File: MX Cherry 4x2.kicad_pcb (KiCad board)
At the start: 2 copper layers, 78.7 x 38.1 mm, 18 parts, among them J1 Conn_01x10_Pin, J2 Conn_01x10_Pin, SW1 SW_Push, SW2 SW_Push, SW3 SW_Push, SW4 SW_Push, SW5 SW_Push, SW6 SW_Push, SW7 SW_Push, SW8 SW_Push

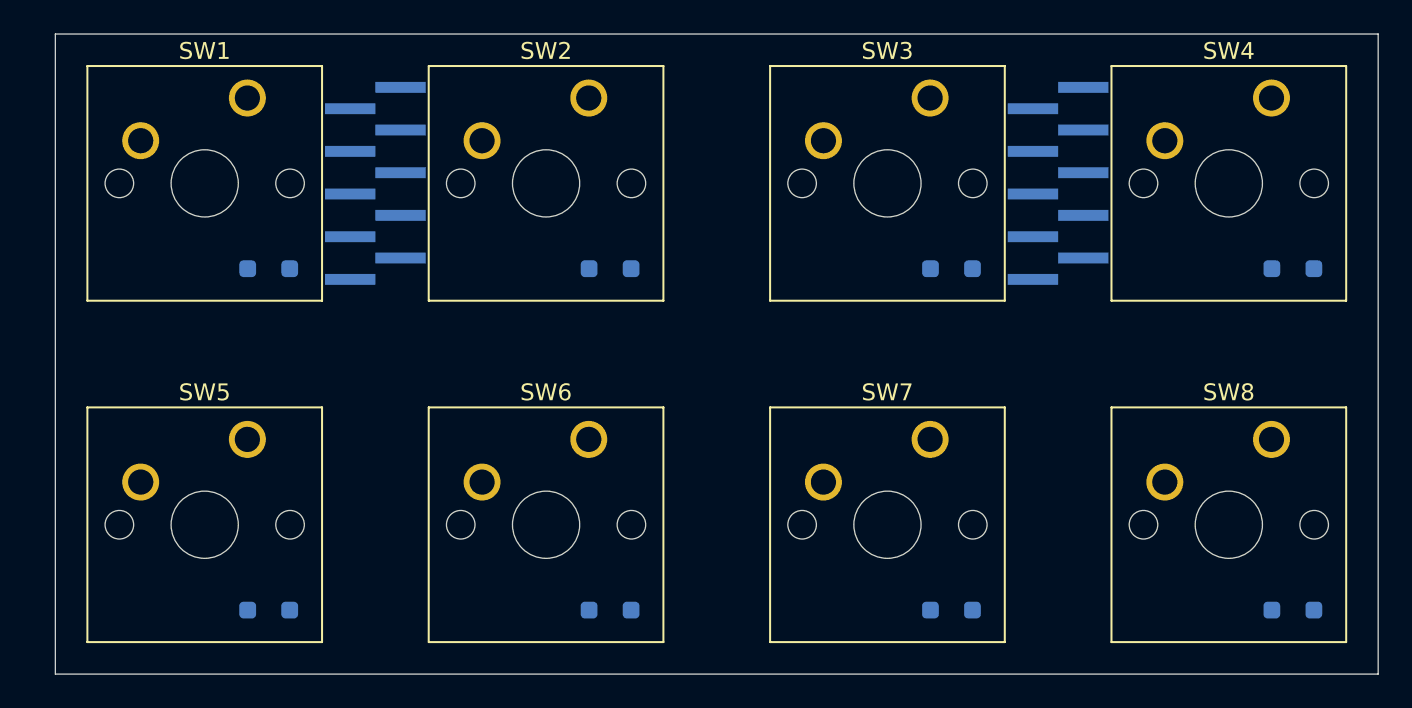
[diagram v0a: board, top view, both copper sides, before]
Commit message: Add LEDs
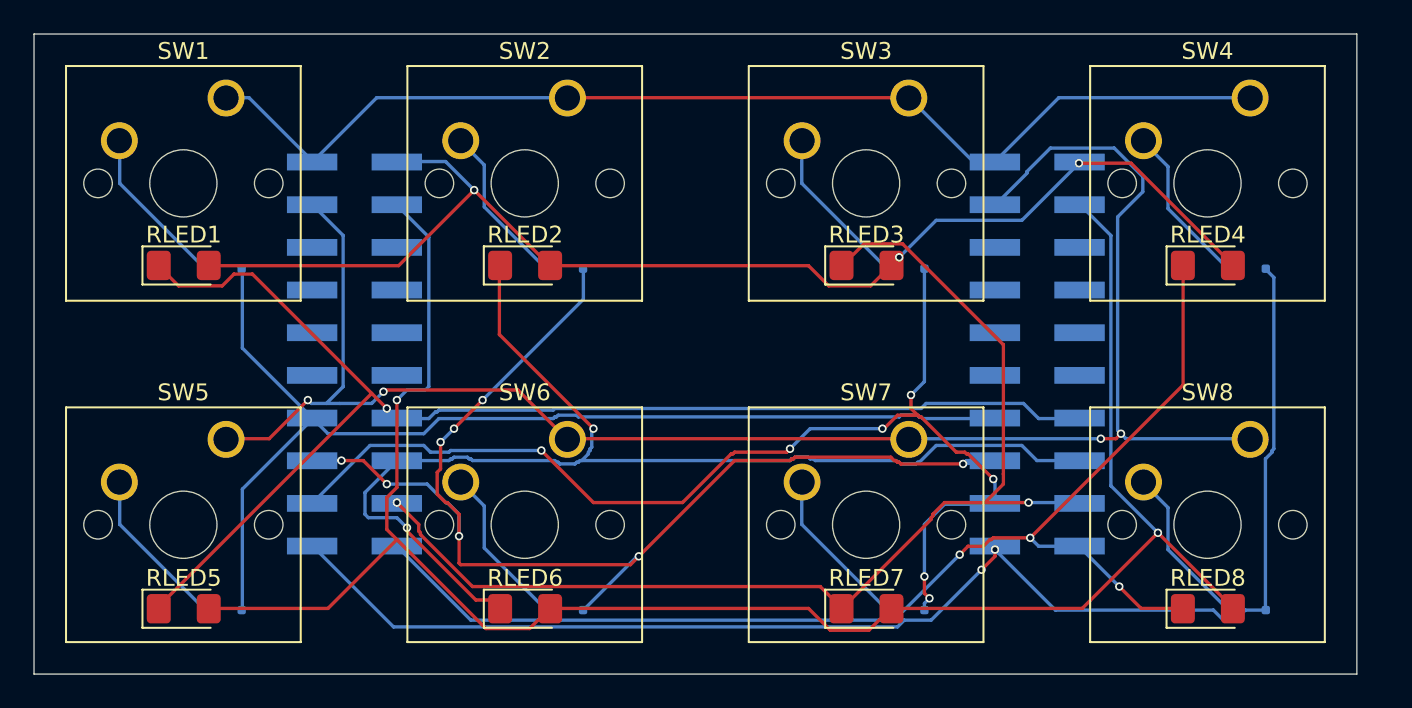
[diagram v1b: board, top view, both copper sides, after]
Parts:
- added RLED1: LED, LED_SMD:LED_1206_3216Metric_Pad1.42x1.75mm_HandSolder, F.Cu at (47.0, 55.7)
- added RLED2: LED, LED_SMD:LED_1206_3216Metric_Pad1.42x1.75mm_HandSolder, F.Cu at (67.3, 55.7)
- added RLED3: LED, LED_SMD:LED_1206_3216Metric_Pad1.42x1.75mm_HandSolder, F.Cu at (87.7, 55.7)
- added RLED4: LED, LED_SMD:LED_1206_3216Metric_Pad1.42x1.75mm_HandSolder, F.Cu at (108.0, 55.7)
- added RLED5: LED, LED_SMD:LED_1206_3216Metric_Pad1.42x1.75mm_HandSolder, F.Cu at (47.0, 76.1)
- added RLED6: LED, LED_SMD:LED_1206_3216Metric_Pad1.42x1.75mm_HandSolder, F.Cu at (67.3, 76.1)
- added RLED7: LED, LED_SMD:LED_1206_3216Metric_Pad1.42x1.75mm_HandSolder, F.Cu at (87.7, 76.1)
- added RLED8: LED, LED_SMD:LED_1206_3216Metric_Pad1.42x1.75mm_HandSolder, F.Cu at (108.0, 76.1)
- D1, D2, D3, D4, D5, D6, D7, D8: footprint Diode_SMD:D_SOD-323_HandSoldering -> Diode_SMD:D_SOD-323F
- J1, J2: value Conn_01x10_Pin -> Conn_02x10_Odd_Even; footprint Connector_PinHeader_1.27mm:PinHeader_1x10_P1.27mm_Vertical_SMD_Pin1Left -> Connector_PinSocket_2.54mm:PinSocket_2x10_P2.54mm_Vertical_SMD
- moved J2 43.1 mm to (57.2, 61.0)
- moved J1 40.7 mm to (97.8, 61.0)
- moved D4 2.71 mm to (110.3, 55.9)
- moved D8 2.71 mm to (110.3, 76.2)
- moved D1 2.71 mm to (49.4, 55.9)
- moved D5 2.71 mm to (49.4, 76.2)
- moved D2 2.71 mm to (69.7, 55.9)
- moved D3 2.71 mm to (90.0, 55.9)
- moved D6 2.71 mm to (69.7, 76.2)
- moved D7 2.71 mm to (90.0, 76.2)
- moved SW2 1.27 mm to (69.8, 45.7)
- moved SW4 1.27 mm to (110.5, 45.7)
- moved SW6 1.27 mm to (69.8, 66.0)
- moved SW8 1.27 mm to (110.5, 66.0)
- moved SW1 1.27 mm to (49.5, 45.7)
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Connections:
- D1 pad 1: COL_0 -> SW_0_COL_0
- D2 pad 1: COL_1 -> SW_0_COL_1
- D3 pad 1: COL_2 -> SW_0_COL_2
- D4 pad 1: COL_3 -> SW_0_COL_3
- D5 pad 1: COL_0 -> SW_0_COL_0
- D6 pad 1: COL_1 -> SW_0_COL_1
- D7 pad 1: COL_2 -> SW_0_COL_2
- D8 pad 1: COL_3 -> SW_0_COL_3
- J1 pad 1: COL_0 -> SW_0_ROW_0
- J1 pad 2: COL_1 -> LED_0_ROW_0
- J1 pad 3: COL_2 -> SW_0_ROW_1
- J1 pad 4: COL_3 -> LED_0_ROW_1
- J1 pad 5: ROW_0 -> unconnected-(J1-Pin_5-Pad5)
- J1 pad 6: ROW_1 -> unconnected-(J1-Pin_6-Pad6)
- J2 pad 1: COL_0 -> SW_0_ROW_0
- J2 pad 2: COL_1 -> LED_0_ROW_0
- J2 pad 3: COL_2 -> SW_0_ROW_1
- J2 pad 4: COL_3 -> LED_0_ROW_1
- J2 pad 5: ROW_0 -> unconnected-(J2-Pin_5-Pad5)
- J2 pad 6: ROW_1 -> unconnected-(J2-Pin_6-Pad6)
- SW1 pad 1: ROW_0 -> SW_0_ROW_0
- SW2 pad 1: ROW_0 -> SW_0_ROW_0
- SW3 pad 1: ROW_0 -> SW_0_ROW_0
- SW4 pad 1: ROW_0 -> SW_0_ROW_0
- SW5 pad 1: ROW_1 -> SW_0_ROW_1
- SW6 pad 1: ROW_1 -> SW_0_ROW_1
- SW7 pad 1: ROW_1 -> SW_0_ROW_1
- SW8 pad 1: ROW_1 -> SW_0_ROW_1
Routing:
- net LED_0_ROW_1: track 0.00 -> 114.5 mm, vias 0 -> 2
- net SW_0_ROW_1: track 0.00 -> 103.8 mm, vias 0 -> 4
- net SW_0_COL_3: track 0.00 -> 83.8 mm, vias 0 -> 2
- net LED_0_COL_0: track 0.00 -> 78.1 mm, vias 0 -> 1
- net LED_0_ROW_0: track 0.00 -> 76.2 mm, vias 0 -> 3
- net SW_0_COL_1: track 0.00 -> 74.6 mm, vias 0 -> 8
- net LED_0_COL_3: track 0.00 -> 72.4 mm, vias 0 -> 3
- net LED_0_COL_1: track 0.00 -> 70.8 mm, vias 0 -> 2
- net LED_0_COL_2: track 0.00 -> 68.8 mm, vias 0 -> 2
- net SW_0_COL_2: track 0.00 -> 67.9 mm, vias 0 -> 7
- net SW_0_ROW_0: track 0.00 -> 67.4 mm
- net SW_0_COL_0: track 0.00 -> 65.5 mm
- net Net-(D1-A): track 0.00 -> 9.76 mm
- net Net-(D5-A): track 0.00 -> 9.75 mm
- net Net-(D4-A): track 0.00 -> 9.74 mm
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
